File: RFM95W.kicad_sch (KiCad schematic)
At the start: 3 parts, among them U7 RFM95W-915S2

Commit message: Most post v0.2.0 fixes done. About to mess with GND_ANT zone and net.
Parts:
- removed AE1: 915mhz antenna, ProjectLib:915MHz_spring_antenna, symbol Device:Antenna
- added AE1: Antenna_Shield, ProjectLib:U.FL_Molex_MCRF_73412-0110_Vertical, symbol ProjectLib:Antenna_Shield
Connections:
- net GND: now also AE1.2 (Shield)
- net at U7.9 (ANT): now also AE1.1 (A)
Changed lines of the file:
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@@
-	)
-	(symbol
-		(lib_id "Device:Antenna")
-		(at 128.27 72.39 0)
-		(unit 1)
-		(exclude_from_sim no)
-		(in_bom yes)
-		(on_board yes)
-		(dnp yes)
-		(property "Reference" "AE1"
-			(at 131.064 68.834 0)
-			(effects
-				(font
-					(size 1.27 1.27)
-				)
-				(justify left)
-			)
-		)
-		(property "Value" "915mhz antenna"
-			(at 130.302 70.866 0)
-			(effects
-				(font
-					(size 1.27 1.27)
-				)
-				(justify left)
-			)
-		)
-		(property "Footprint" "ProjectLib:915MHz_spring_antenna"
-			(at 128.27 72.39 0)
-			(effects
-				(font
-					(size 1.27 1.27)
-				)
-				(hide yes)
-			)
-		)
-		(property "Datasheet" "https://www.nicerf.com/rf-antenna/915mhz-spring-antenna-sw915-th06.html"
-			(at 128.27 72.39 0)
-			(effects
-				(font
-					(size 1.27 1.27)
-				)
-				(hide yes)
-			)
-		)
-		(property "Description" "spring antenna"
-			(at 128.27 72.39 0)
-			(effects
-				(font
-					(size 1.27 1.27)
-				)
-				(hide yes)
-			)
-		)
-		(property "Manufacturer" "G-NiceRF"
-			(at 128.27 72.39 0)
-			(effects
-				(font
-					(size 1.27 1.27)
-				)
-				(hide yes)
-			)
-		)
-		(property "MfgPart" "SW915-TH06"
-			(at 128.27 72.39 0)
-			(effects
-				(font
-					(size 1.27 1.27)
-				)
-				(hide yes)
-			)
-		)
-		(property "MountType" "PTH"
-			(at 128.27 72.39 0)
-			(effects
-				(font
-					(size 1.27 1.27)
-				)
-				(hide yes)
-			)
-		)
-		(property "Notes" "or equivalent"
-			(at 128.27 72.39 0)
-			(effects
-				(font
-					(size 1.27 1.27)
-				)
-				(hide yes)
-			)
-		)
-		(property "pads" "1"
-			(at 128.27 72.39 0)
-			(effects
-				(font
-					(size 1.27 1.27)
-				)
-				(hide yes)
-			)
-		)
-		(pin "1"
-		)
-		(instances
-			(project "SensorProject_t16-pcb"
-				(path "/0c2d0c14-8850-4a30-bb78-b2f40cb442ba/2db29b35-1005-45eb-b852-0b853354466f"
-					(reference "AE1")
-					(unit 1)
-				)
-			)
-		)
 	)
 	(symbol
@@
 					(unit 1)
 				)
+			)
+		)
+	)
+	(symbol
+		(lib_id "power:GND")
+		(at 130.81 77.47 0)
+		(unit 1)
+		(exclude_from_sim no)
+		(in_bom yes)
+		(on_board yes)
+		(dnp no)
+		(fields_autoplaced yes)
+		(property "Reference" "#PWR065"
+			(at 130.81 83.82 0)
+			(effects
+				(font
+					(size 1.27 1.27)
+				)
+				(hide yes)
+			)
+		)
+		(property "Value" "GND"
+			(at 130.81 82.55 0)
+			(effects
+				(font
+					(size 1.27 1.27)
+				)
+			)
+		)
+		(property "Footprint" ""
+			(at 130.81 77.47 0)
+			(effects
+				(font
+					(size 1.27 1.27)
+				)
+				(hide yes)
+			)
+		)
+		(property "Datasheet" ""
+			(at 130.81 77.47 0)
+			(effects
+				(font
+					(size 1.27 1.27)
+				)
+				(hide yes)
+			)
+		)
+		(property "Description" "Power symbol creates a global label with name \"GND\" , ground"
+			(at 130.81 77.47 0)
+			(effects
+				(font
+					(size 1.27 1.27)
+				)
+				(hide yes)
+			)
+		)
+		(pin "1"
+		)
+		(instances
+			(project ""
+				(path "/0c2d0c14-8850-4a30-bb78-b2f40cb442ba/2db29b35-1005-45eb-b852-0b853354466f"
+					(reference "#PWR065")
+					(unit 1)
+				)
+			)
+		)
+	)
+	(symbol
+		(lib_id "ProjectLib:Antenna_Shield")
+		(at 128.27 72.39 0)
+		(unit 1)
+		(exclude_from_sim no)
+		(in_bom yes)
+		(on_board yes)
+		(dnp no)
+		(property "Reference" "AE1"
+			(at 131.318 69.342 0)
+			(effects
+				(font
+					(size 1.27 1.27)
+				)
+				(justify left)
+			)
+		)
+		(property "Value" "Antenna_Shield"
+			(at 126.492 65.024 0)
+			(effects
+				(font
+					(size 1.27 1.27)
+				)
+				(justify left)
+			)
+		)
+		(property "Footprint" "ProjectLib:U.FL_Molex_MCRF_73412-0110_Vertical"
+			(at 128.27 69.85 0)
+			(effects
+				(font
+					(size 1.27 1.27)
+				)
+				(hide yes)
+			)
+		)
+		(property "Datasheet" "~"
+			(at 128.27 69.85 0)
+			(effects
+				(font
+					(size 1.27 1.27)
+				)
+				(hide yes)
+			)
+		)
+		(property "Description" "Antenna with extra pin for shielding"
+			(at 128.27 72.39 0)
+			(effects
+				(font
+					(size 1.27 1.27)
+				)
+				(hide yes)
+			)
+		)
+		(pin "2"
+		)
+		(pin "1"
+		)
+		(instances
+			(project ""
+				(path "/0c2d0c14-8850-4a30-bb78-b2f40cb442ba/2db29b35-1005-45eb-b852-0b853354466f"
+					(reference "AE1")
+					(unit 1)
+				)

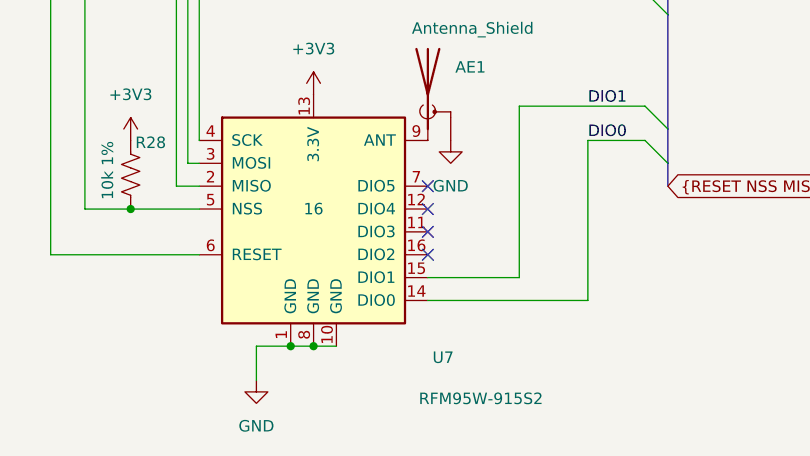
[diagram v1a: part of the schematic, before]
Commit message: Added U.FL for antenna, with GND_ANT zone.
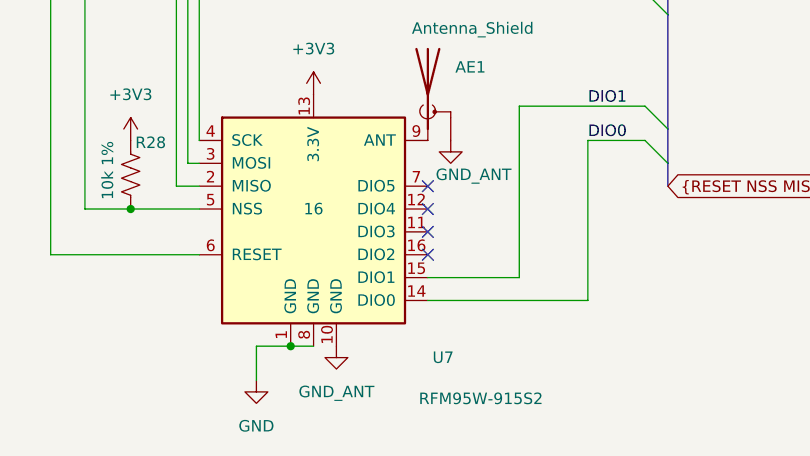
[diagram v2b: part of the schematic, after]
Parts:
- AE1: Manufacturer (none) -> Hirose; MfgPart (none) -> U.FL-R-SMT-1; MountType (none) -> SMT; Notes (none) -> or equivalent
- R28: symbol Device:R_US -> ProjectLib:R_US
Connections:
- net GND: no longer AE1.2 (Shield), U7.10 (GND)
- new net GND_ANT: AE1.2 (Shield), U7.10 (GND)
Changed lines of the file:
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@@
-	)
-	(junction
-		(at 115.57 100.33)
-		(diameter 0)
-		(color 0 0 0 0)
 	)
 	(junction
@@
 		(pts
 			(xy 154.94 63.5) (xy 154.94 76.2)
-		)
-		(stroke
-			(width 0)
-			(type default)
-		)
-	)
-	(wire
-		(pts
-			(xy 115.57 100.33) (xy 118.11 100.33)
 		)
 		(stroke
@@
 	)
 	(symbol
-		(lib_id "Device:R_US")
+		(lib_id "ProjectLib:R_US")
 		(at 95.25 81.28 0)
 		(unit 1)
@@
 			)
 		)
-		(property "Datasheet" ""
+		(property "Datasheet" "~"
 			(at 95.25 81.28 0)
 			(effects
@@
 				(path "/0c2d0c14-8850-4a30-bb78-b2f40cb442ba/2db29b35-1005-45eb-b852-0b853354466f"
 					(reference "R28")
+					(unit 1)
+				)
+			)
+		)
+	)
+	(symbol
+		(lib_id "ProjectLib:GND_ANT")
+		(at 118.11 100.33 0)
+		(unit 1)
+		(exclude_from_sim no)
+		(in_bom yes)
+		(on_board yes)
+		(dnp no)
+		(fields_autoplaced yes)
+		(property "Reference" "#PWR066"
+			(at 118.11 106.68 0)
+			(effects
+				(font
+					(size 1.27 1.27)
+				)
+				(hide yes)
+			)
+		)
+		(property "Value" "GND_ANT"
+			(at 118.11 105.41 0)
+			(effects
+				(font
+					(size 1.27 1.27)
+				)
+			)
+		)
+		(property "Footprint" ""
+			(at 118.11 100.33 0)
+			(effects
+				(font
+					(size 1.27 1.27)
+				)
+				(hide yes)
+			)
+		)
+		(property "Datasheet" ""
+			(at 118.11 100.33 0)
+			(effects
+				(font
+					(size 1.27 1.27)
+				)
+				(hide yes)
+			)
+		)
+		(property "Description" "Power symbol creates a global label with name \"GND_ANT\" , ground"
+			(at 118.11 100.33 0)
+			(effects
+				(font
+					(size 1.27 1.27)
+				)
+				(hide yes)
+			)
+		)
+		(pin "1"
+		)
+		(instances
+			(project ""
+				(path "/0c2d0c14-8850-4a30-bb78-b2f40cb442ba/2db29b35-1005-45eb-b852-0b853354466f"
+					(reference "#PWR066")
+					(unit 1)
+				)
+			)
+		)
+	)
+	(symbol
+		(lib_id "ProjectLib:GND_ANT")
+		(at 130.81 77.47 0)
+		(unit 1)
+		(exclude_from_sim no)
+		(in_bom yes)
+		(on_board yes)
+		(dnp no)
+		(property "Reference" "#PWR065"
+			(at 130.81 83.82 0)
+			(effects
+				(font
+					(size 1.27 1.27)
+				)
+				(hide yes)
+			)
+		)
+		(property "Value" "GND_ANT"
+			(at 133.35 81.28 0)
+			(effects
+				(font
+					(size 1.27 1.27)
+				)
+			)
+		)
+		(property "Footprint" ""
+			(at 130.81 77.47 0)
+			(effects
+				(font
+					(size 1.27 1.27)
+				)
+				(hide yes)
+			)
+		)
+		(property "Datasheet" ""
+			(at 130.81 77.47 0)
+			(effects
+				(font
+					(size 1.27 1.27)
+				)
+				(hide yes)
+			)
+		)
+		(property "Description" "Power symbol creates a global label with name \"GND_ANT\" , ground"
+			(at 130.81 77.47 0)
+			(effects
+				(font
+					(size 1.27 1.27)
+				)
+				(hide yes)
+			)
+		)
+		(pin "1"
+		)
+		(instances
+			(project ""
+				(path "/0c2d0c14-8850-4a30-bb78-b2f40cb442ba/2db29b35-1005-45eb-b852-0b853354466f"
+					(reference "#PWR065")
 					(unit 1)
 				)
@@
 			)
 		)
-		(property "Datasheet" "https://www.hoperf.com/data/upload/portal/20181127/5bfcbea20e9ef.pdf"
+		(property "Datasheet" "https://cdn.sparkfun.com/assets/learn_tutorials/8/0/4/RFM95_96_97_98W.pdf"
 			(at 31.75 43.18 0)
 			(effects
@@
 			)
 		)
-		(property "Description" "LoRa module, SPI, 915 MHz"
+		(property "Description" "Low power long range transceiver module, SPI and parallel interface, 915 MHz, spreading factor 6 to12, bandwidth 7.8 to 500kHz, -111 to -148 dBm, SMD-16, DIP-16"
 			(at 115.57 85.09 0)
 			(effects
@@
 				(path "/0c2d0c14-8850-4a30-bb78-b2f40cb442ba/2db29b35-1005-45eb-b852-0b853354466f"
 					(reference "U7")
-					(unit 1)
-				)
-			)
-		)
-	)
-	(symbol
-		(lib_id "power:GND")
-		(at 130.81 77.47 0)
-		(unit 1)
-		(exclude_from_sim no)
-		(in_bom yes)
-		(on_board yes)
-		(dnp no)
-		(fields_autoplaced yes)
-		(property "Reference" "#PWR065"
-			(at 130.81 83.82 0)
-			(effects
-				(font
-					(size 1.27 1.27)
-				)
-				(hide yes)
-			)
-		)
-		(property "Value" "GND"
-			(at 130.81 82.55 0)
-			(effects
-				(font
-					(size 1.27 1.27)
-				)
-			)
-		)
-		(property "Footprint" ""
-			(at 130.81 77.47 0)
-			(effects
-				(font
-					(size 1.27 1.27)
-				)
-				(hide yes)
-			)
-		)
-		(property "Datasheet" ""
-			(at 130.81 77.47 0)
-			(effects
-				(font
-					(size 1.27 1.27)
-				)
-				(hide yes)
-			)
-		)
-		(property "Description" "Power symbol creates a global label with name \"GND\" , ground"
-			(at 130.81 77.47 0)
-			(effects
-				(font
-					(size 1.27 1.27)
-				)
-				(hide yes)
-			)
-		)
-		(pin "1"
-		)
-		(instances
-			(project ""
-				(path "/0c2d0c14-8850-4a30-bb78-b2f40cb442ba/2db29b35-1005-45eb-b852-0b853354466f"
-					(reference "#PWR065")
 					(unit 1)
 				)
@@
 			)
 		)
-		(property "Datasheet" "~"
+		(property "Datasheet" "https://www.hirose.com/en/product/document?clcode=CL0331-0472-2-60&productname=U.FL-R-SMT-1(60)&series=U.FL&documenttype=Catalog&lang=en&documentid=ed_U.FL_CAT"
 			(at 128.27 69.85 0)
 			(effects
@@
 			(at 128.27 72.39 0)
 			(effects
+				(font
+					(size 1.27 1.27)
+				)
+				(hide yes)
+			)
+		)
+		(property "Manufacturer" "Hirose"
+			(at 128.27 72.39 0)
+			(effects
+				(font
+					(size 1.27 1.27)
+				)
+				(hide yes)
+			)
+		)
+		(property "MfgPart" "U.FL-R-SMT-1"
+			(at 128.27 72.39 0)
+			(effects
+				(font
+					(size 1.27 1.27)
+				)
+				(hide yes)
+			)
+		)
+		(property "Notes" "or equivalent"
+			(at 128.27 72.39 0)
+			(effects
+				(font
+					(size 1.27 1.27)
+				)
+				(hide yes)
+			)
+		)
+		(property "MountType" "SMT"
+			(at 128.27 72.39 0)
+			(effects

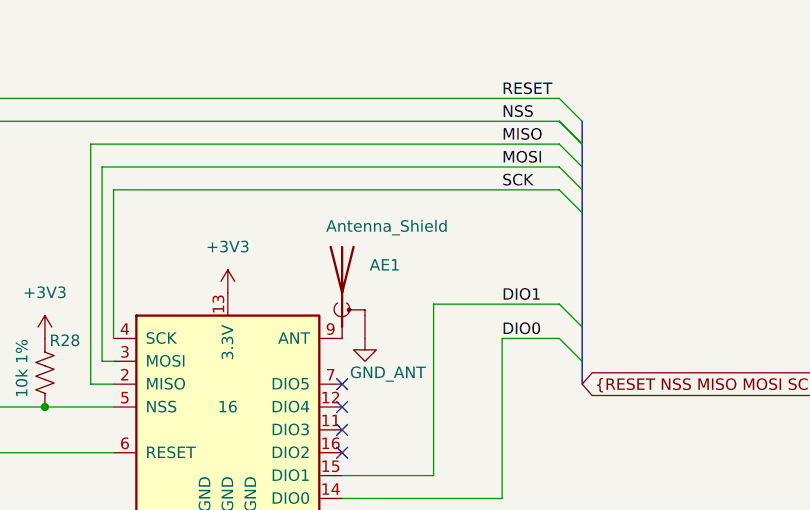
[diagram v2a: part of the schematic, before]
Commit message: BOM cleaned up.
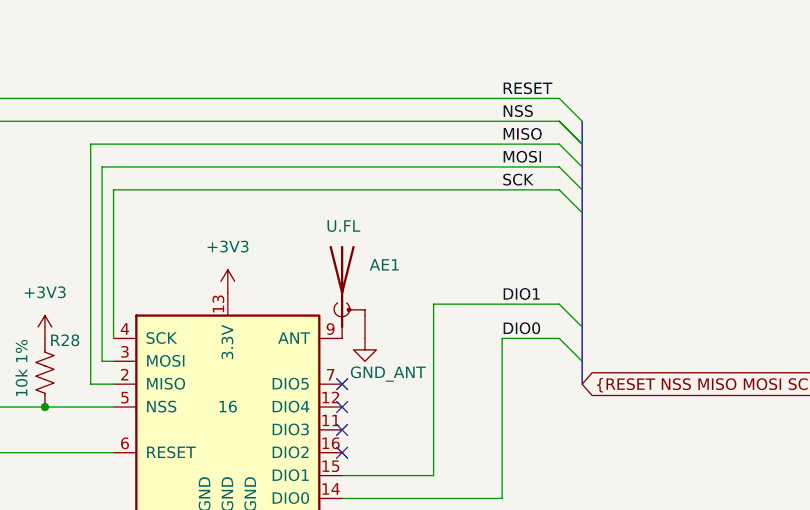
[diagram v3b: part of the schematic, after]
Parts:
- AE1: value Antenna_Shield -> U.FL
- R28: Notes (none) -> or equivalent; Package (none) -> R_0603_1608Metric
- U7: Package (none) -> HOPERF_RFM9XW_SMD
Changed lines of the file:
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@@
 			)
 		)
-		(property "Datasheet" "~"
+		(property "Datasheet" ""
 			(at 95.25 81.28 0)
 			(effects
@@
 		)
 		(property "MfgPart" "CRCW060310K0FKEA"
+			(at 95.25 81.28 0)
+			(effects
+				(font
+					(size 1.27 1.27)
+				)
+				(hide yes)
+			)
+		)
+		(property "Package" "R_0603_1608Metric"
+			(at 95.25 81.28 0)
+			(effects
+				(font
+					(size 1.27 1.27)
+				)
+				(hide yes)
+			)
+		)
+		(property "Notes" "or equivalent"
 			(at 95.25 81.28 0)
 			(effects
@@
 			)
 		)
-		(property "Description" "Low power long range transceiver module, SPI and parallel interface, 915 MHz, spreading factor 6 to12, bandwidth 7.8 to 500kHz, -111 to -148 dBm, SMD-16, DIP-16"
+		(property "Description" "LoRa module, SPI, 915 MHz,  SMD-16"
 			(at 115.57 85.09 0)
 			(effects
@@
 					(size 1.27 1.27)
 				)
+			)
+		)
+		(property "Package" "HOPERF_RFM9XW_SMD"
+			(at 115.57 85.09 0)
+			(effects
+				(font
+					(size 1.27 1.27)
+				)
+				(hide yes)
 			)
 		)
@@
 			)
 		)
-		(property "Value" "Antenna_Shield"
+		(property "Value" "U.FL"
 			(at 126.492 65.024 0)
 			(effects
@@
 			(at 128.27 72.39 0)
 			(effects
+				(font
+					(size 1.27 1.27)
+				)
+				(hide yes)
+			)
+		)
+		(property "Package" ""
+			(at 128.27 72.39 0)
+			(effects

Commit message: converted R, C, and L to smaller 0402 footprints. Some trace rearranging and cleanup.
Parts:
- R28: footprint ProjectLib:R_0603_1608Metric -> ProjectLib:R_0402_1005Metric; Manufacturer Vishay -> (none); MfgPart CRCW060310K0FKEA -> (none); Package R_0603_1608Metric -> R_0402_1005Metric
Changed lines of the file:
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@@
 			)
 		)
-		(property "Footprint" "ProjectLib:R_0603_1608Metric"
+		(property "Footprint" "ProjectLib:R_0402_1005Metric"
 			(at 96.266 81.534 90)
 			(effects
@@
 			)
 		)
-		(property "Manufacturer" "Vishay"
+		(property "Manufacturer" ""
 			(at 95.25 81.28 0)
 			(effects
@@
 			)
 		)
-		(property "MfgPart" "CRCW060310K0FKEA"
+		(property "MfgPart" ""
 			(at 95.25 81.28 0)
 			(effects
@@
 			)
 		)
-		(property "Package" "R_0603_1608Metric"
+		(property "Package" "R_0402_1005Metric"
 			(at 95.25 81.28 0)
 			(effects

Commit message: some (documentation) cleanup while submitting for fabrication.
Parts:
- AE1: Package (none) -> U.FL
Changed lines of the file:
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@@
 			)
 		)
-		(property "Description" "Antenna with extra pin for shielding"
+		(property "Description" "Antenna connector with shielding"
 			(at 128.27 72.39 0)
 			(effects
@@
 			)
 		)
-		(property "Package" ""
+		(property "Package" "U.FL"
 			(at 128.27 72.39 0)
 			(effects

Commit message: v0.2.2 with BOM fixes, some additional documentation and cleanup.
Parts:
- AE1: MfgPart U.FL-R-SMT-1 -> U.FL-R-SMT-K(800)
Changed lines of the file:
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@@
 			)
 		)
-		(property "Datasheet" "https://www.hirose.com/en/product/document?clcode=CL0331-0472-2-60&productname=U.FL-R-SMT-1(60)&series=U.FL&documenttype=Catalog&lang=en&documentid=ed_U.FL_CAT"
+		(property "Datasheet" "https://www.hirose.com/en/product/p/CL0480-0761-0-00"
 			(at 128.27 69.85 0)
 			(effects
@@
 			)
 		)
-		(property "MfgPart" "U.FL-R-SMT-1"
+		(property "MfgPart" "U.FL-R-SMT-K(800)"
 			(at 128.27 72.39 0)
 			(effects

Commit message: improved schematic sheet titles.
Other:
- title: ADCs for 10K thermistors -> RFM95W 915MHz
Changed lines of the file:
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@@
 	(paper "A4")
 	(title_block
-		(title "ADCs for 10K thermistors")
-		(date "2025-01-07")
-		(rev "v0.1.1")
+		(title "RFM95W 915MHz")
+		(date "2025-09-15")
+		(rev "v0.2.2")
 	)
 	(bus_alias "SPI"
